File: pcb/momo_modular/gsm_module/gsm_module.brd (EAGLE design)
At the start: 50.8 x 33 mm, 19 parts, among them U1 PIC16LF1823, U2 TI-HIGHSIDE-PFET, U3 SIM900, U4 ESD-SMF05C

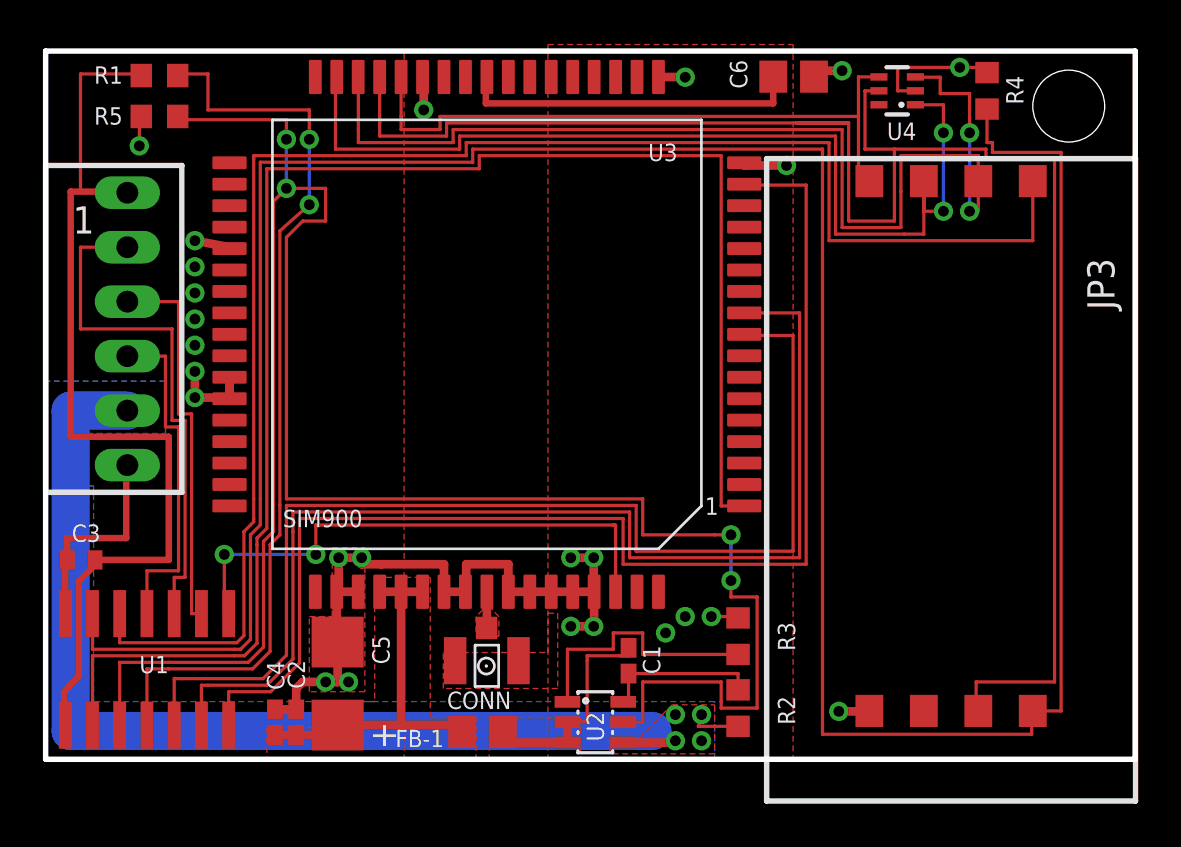
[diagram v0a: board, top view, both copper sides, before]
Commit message: Fix gsm layout based on measured SIM900 module size.
U1 and C5 would be very close to the module so I relaid it out in
order to maximize the distance between the SIM900 and those two
components.  Also, C5 was swapped for a smaller tantalum capacitor
since the ripple current was calculated too conservatively last time.
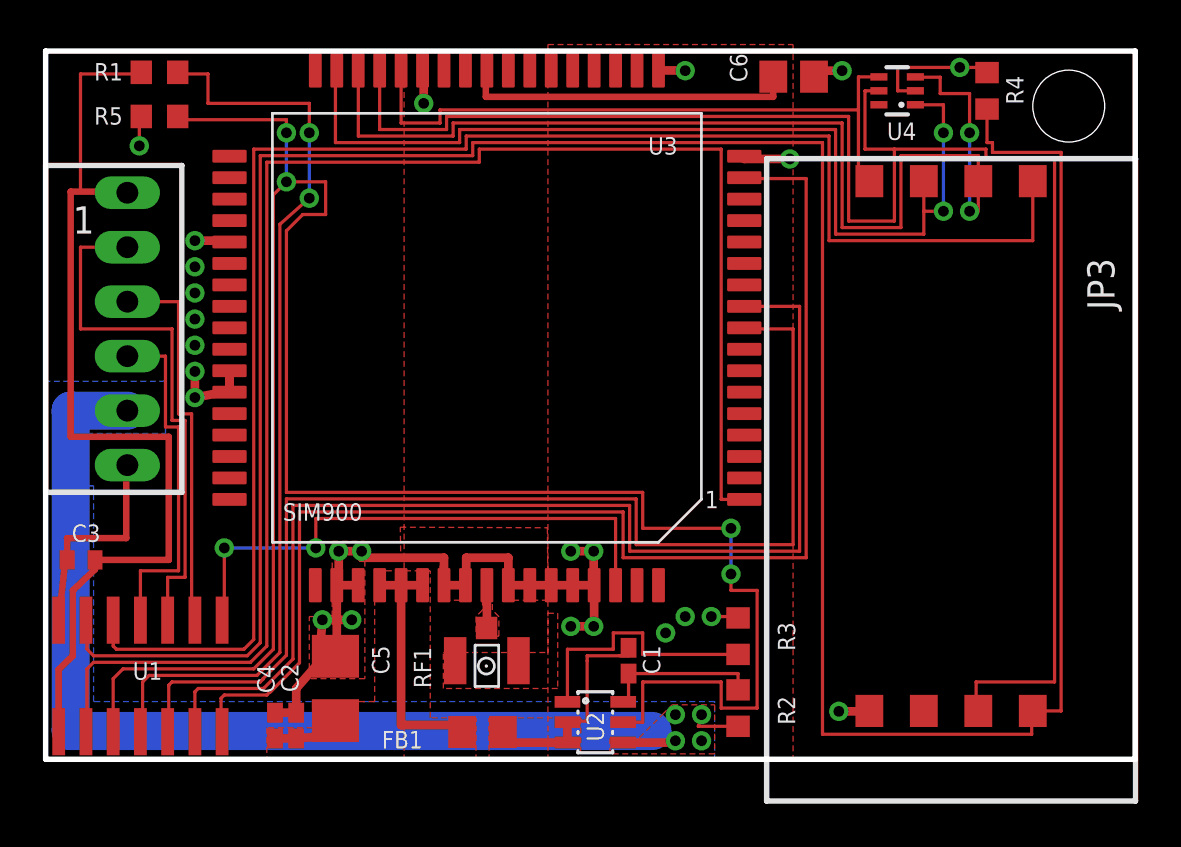
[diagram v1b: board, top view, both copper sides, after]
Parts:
- C5: value 330 uF -> 220 uF; device components:2917 -> rcl:CT3528
- moved U1 0.43 mm to (9.50, 8.97)
- moved U3 0.30 mm to (25.7, 25.2)
- moved C5 0.25 mm to (18.6, 8.38), turned to 90 degrees
- moved C2 0.15 mm to (16.8, 6.65)
- moved C4 0.15 mm to (15.8, 6.65)
- moved R1 0.15 mm to (10.4, 37.1)
- renumbered CONN to RF1, FB-1 to FB1
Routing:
- net VDD: track 17.7 -> 14.6 mm
- net SIMDAT: track 79.9 -> 77.8 mm
- net GND: track 66.6 -> 68.4 mm
- net SW1: track 74.1 -> 75.5 mm
- net SIMRST: track 47.2 -> 46.0 mm
- net SW2: track 129.6 -> 130.7 mm
- net PWRKEY: track 72.7 -> 73.5 mm
- net RESET: track 58.5 -> 59.3 mm
- net POW-SW-ON: track 98.9 -> 99.7 mm
- net RXD: track 53.2 -> 54.0 mm
- net TXD: track 53.0 -> 53.7 mm
- net VCCINT: track 47.1 -> 47.7 mm
- net CLOCK: track 24.7 -> 25.3 mm
- net ALARM: track 15.9 -> 16.5 mm

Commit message: Fix gsm module to not have sim card adapter hang over board edge
- This would have meant that the board could not be routed post
smt assembly and that the board could not have been panelized at
2x1.3" since the part would not have been assemblable.
- As a consequence, I had to get rid of the screw holes for this
module.
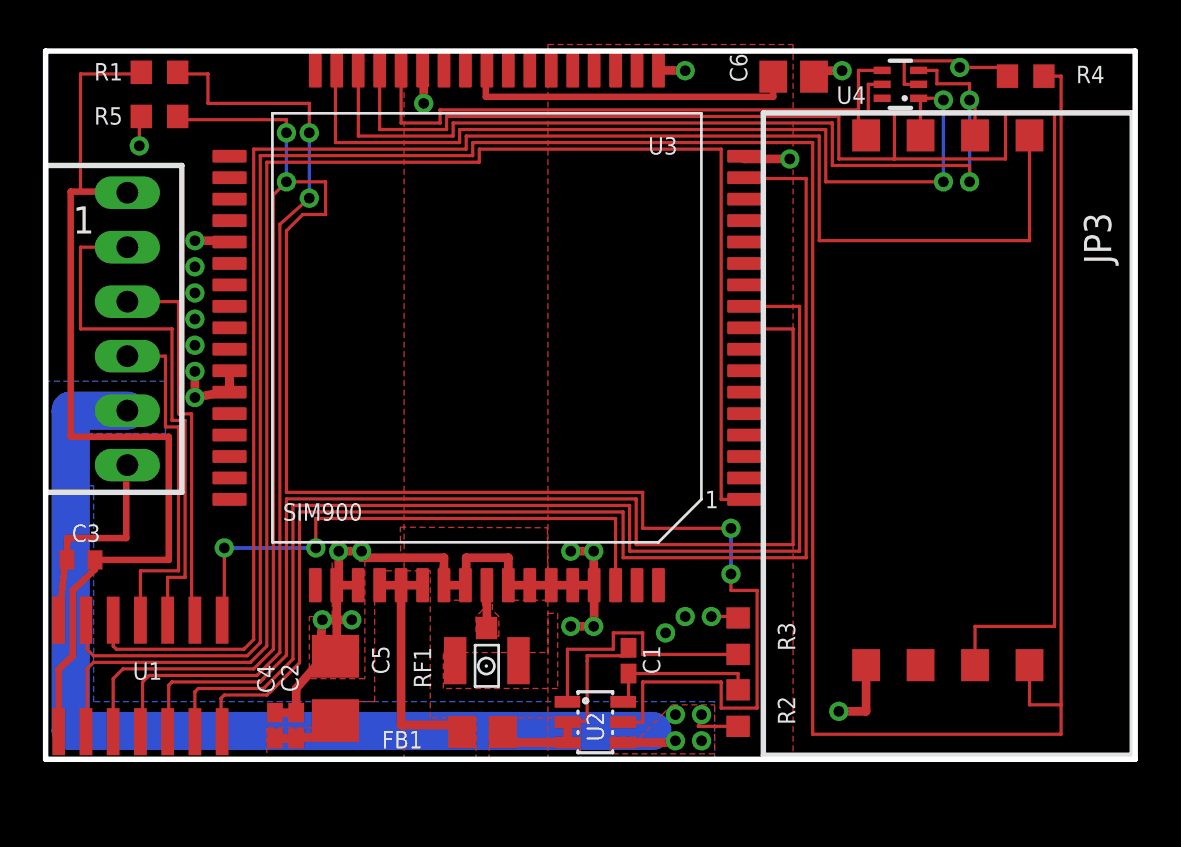
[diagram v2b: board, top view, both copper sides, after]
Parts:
- moved JP3 2.14 mm to (47.1, 21.8)
- moved R4 1.93 mm to (50.8, 36.9), turned to 0 degrees
- moved U4 0.34 mm to (44.9, 36.6)
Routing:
- net SIMCLK: track 52.6 -> 44.4 mm
- net SIMRST: track 46.0 -> 41.8 mm
- net SIMDAT: track 77.8 -> 73.7 mm
- net GND: track 68.4 -> 71.4 mm
- net SW2: track 130.7 -> 132.9 mm
- net SW1: track 75.5 -> 77.4 mm
- net SIMVCC: track 30.7 -> 28.9 mm
